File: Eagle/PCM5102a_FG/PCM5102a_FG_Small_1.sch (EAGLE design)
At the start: 28 parts, among them IC1 PSOC_5LP_PROTOTIYPING_KIT, IC2 PCM5102A, IC3 TA48M033F, Q1 20MHz

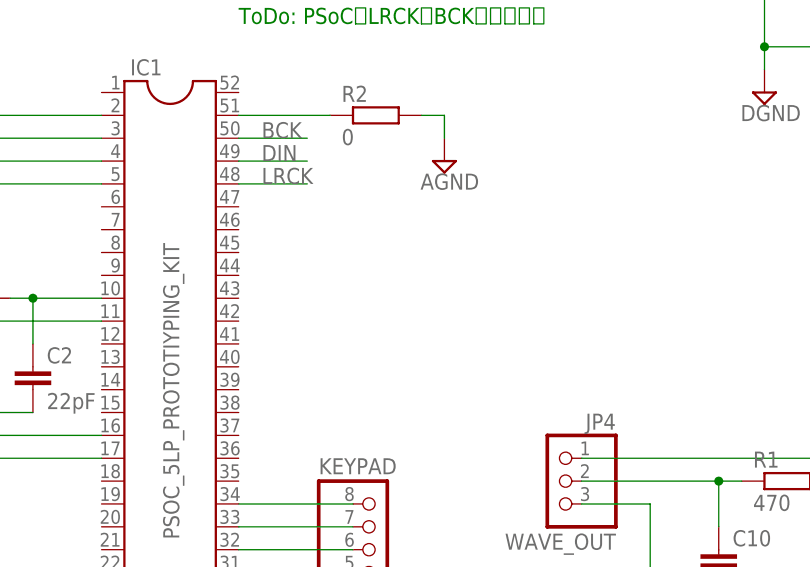
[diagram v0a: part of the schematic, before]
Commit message: 電源電圧測定
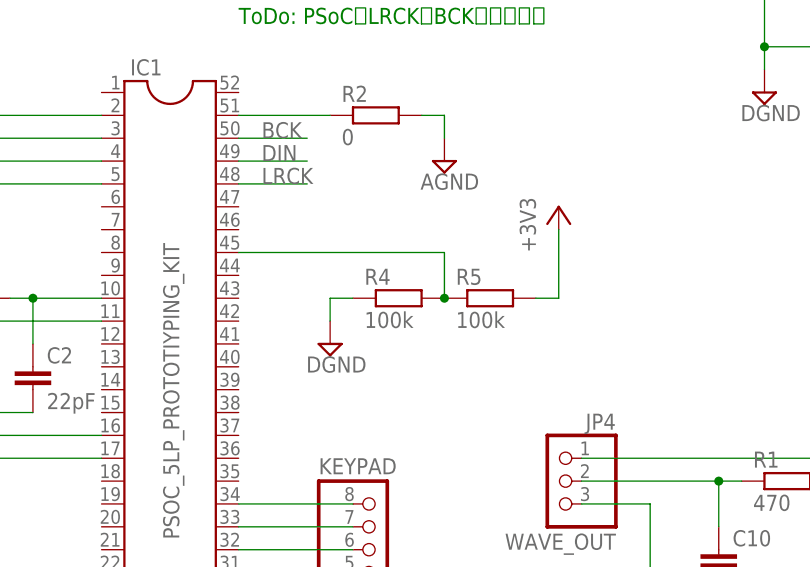
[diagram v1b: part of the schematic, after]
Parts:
- added R4, R5: 100k, resistor:R-EU_0207/7
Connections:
- new net N$19: IC1.45, R4.2, R5.1
- net +3V3: now also R5.2
- net DGND: now also R4.1
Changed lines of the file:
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@@
 <setting verticaltext="up"/>
 </settings>
-<grid distance="0.1" unitdist="inch" unit="inch" style="lines" multiple="1" display="no" altdistance="0.01" altunitdist="inch" altunit="inch"/>
+<grid distance="0.1" unitdist="inch" unit="inch" style="lines" multiple="1" display="yes" altdistance="0.01" altunitdist="inch" altunit="inch"/>
 <layers>
 <layer number="1" name="Top" color="4" fill="1" visible="no" active="no"/>
@@
 <part name="FRAME1" library="frames" deviceset="A4L-LOC" device="" value="PCM5102A_FG"/>
 <part name="C16" library="rcl" deviceset="CPOL-EU" device="E2.5-5" value="10uF"/>
+<part name="R4" library="resistor" deviceset="R-EU_" device="0207/7" value="100k"/>
+<part name="R5" library="resistor" deviceset="R-EU_" device="0207/7" value="100k"/>
+<part name="SUPPLY2" library="supply2" deviceset="DGND" device=""/>
+<part name="+3V5" library="supply1" deviceset="+3V3" device=""/>
 </parts>
 <sheets>
@@
 <instance part="FRAME1" gate="G$1" x="0" y="0"/>
 <instance part="C16" gate="G$1" x="167.64" y="96.52" rot="MR90"/>
+<instance part="R4" gate="G$1" x="104.14" y="91.44"/>
+<instance part="R5" gate="G$1" x="114.3" y="91.44"/>
+<instance part="SUPPLY2" gate="G$1" x="96.52" y="86.36"/>
+<instance part="+3V5" gate="G$1" x="121.92" y="101.6"/>
 </instances>
 <busses>
@@
 <junction x="154.94" y="119.38"/>
 </segment>
+<segment>
+<wire x1="96.52" y1="88.9" x2="96.52" y2="91.44" width="0.1524" layer="91"/>
+<pinref part="R4" gate="G$1" pin="1"/>
+<wire x1="96.52" y1="91.44" x2="99.06" y2="91.44" width="0.1524" layer="91"/>
+<pinref part="SUPPLY2" gate="G$1" pin="DGND"/>
+</segment>
 </net>
 <net name="N$1" class="0">
@@
 <wire x1="208.28" y1="149.86" x2="208.28" y2="139.7" width="0.1524" layer="91"/>
 <junction x="208.28" y="139.7"/>
+</segment>
+<segment>
+<pinref part="R5" gate="G$1" pin="2"/>
+<wire x1="119.38" y1="91.44" x2="121.92" y2="91.44" width="0.1524" layer="91"/>
+<pinref part="+3V5" gate="G$1" pin="+3V3"/>
+<wire x1="121.92" y1="91.44" x2="121.92" y2="99.06" width="0.1524" layer="91"/>
 </segment>
 </net>
@@
 </segment>
 </net>
+<net name="N$19" class="0">
+<segment>
+<pinref part="R4" gate="G$1" pin="2"/>
+<pinref part="R5" gate="G$1" pin="1"/>
+<pinref part="IC1" gate="G$1" pin="45"/>
+<wire x1="86.36" y1="96.52" x2="109.22" y2="96.52" width="0.1524" layer="91"/>
+<wire x1="109.22" y1="96.52" x2="109.22" y2="91.44" width="0.1524" layer="91"/>
+<junction x="109.22" y="91.44"/>
+</segment>
+</net>

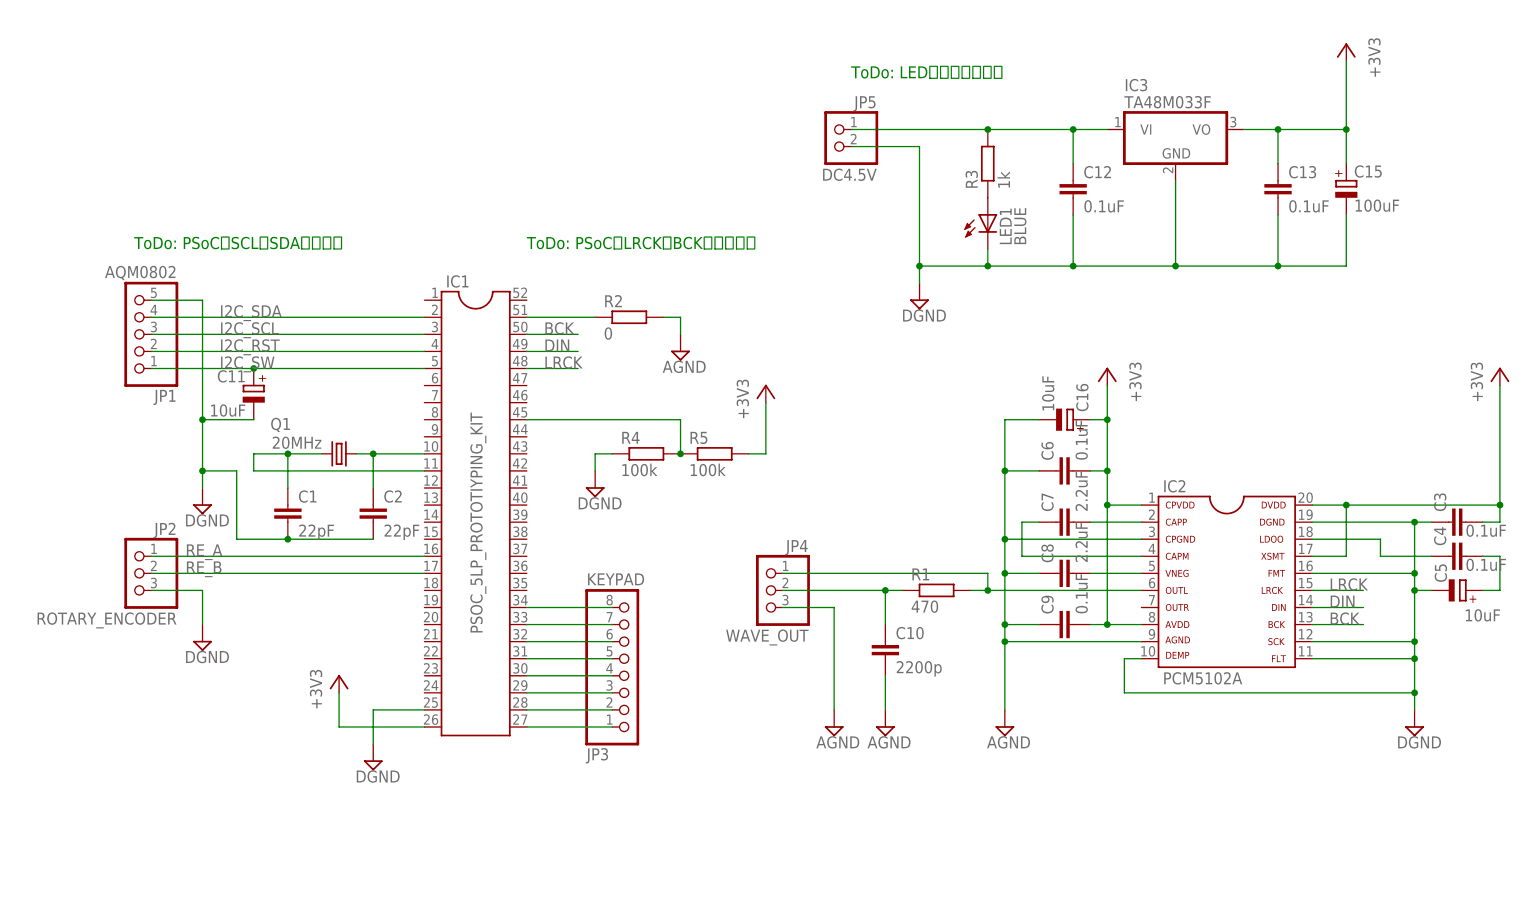
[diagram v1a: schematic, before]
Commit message: LCDのコントラスト調整
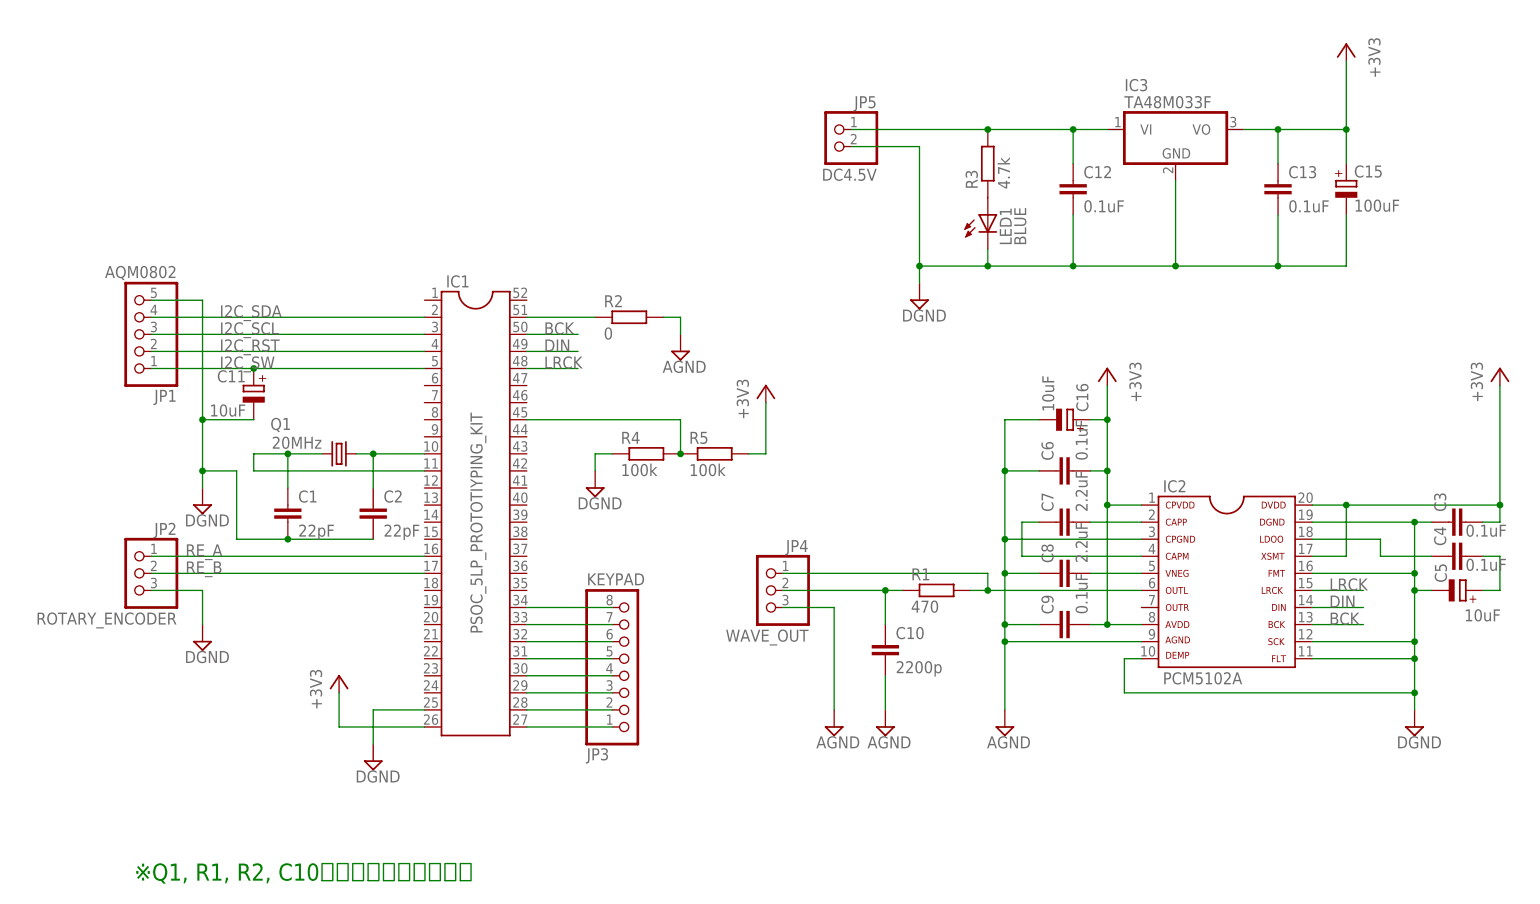
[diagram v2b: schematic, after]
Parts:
- R3: value 1k -> 4.7k
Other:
- note added: "※Q1, R1, R2, C10はピンソケットで実装"
- note removed: "ToDo: LEDの明るさの確認"
- note removed: "ToDo: PSoCでLRCKとBCKを入れ替え"
- note removed: "ToDo: PSoCでSCLとSDA入れ替え"
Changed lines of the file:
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@@
 <setting verticaltext="up"/>
 </settings>
-<grid distance="0.1" unitdist="inch" unit="inch" style="lines" multiple="1" display="yes" altdistance="0.01" altunitdist="inch" altunit="inch"/>
+<grid distance="0.1" unitdist="inch" unit="inch" style="lines" multiple="1" display="no" altdistance="0.01" altunitdist="inch" altunit="inch"/>
 <layers>
 <layer number="1" name="Top" color="4" fill="1" visible="no" active="no"/>
@@
 <part name="+3V2" library="supply1" deviceset="+3V3" device=""/>
 <part name="LED1" library="led" deviceset="LED" device="3MM" value="BLUE"/>
-<part name="R3" library="resistor" deviceset="R-EU_" device="0207/7" value="1k"/>
+<part name="R3" library="resistor" deviceset="R-EU_" device="0207/7" value="4.7k"/>
 <part name="FRAME1" library="frames" deviceset="A4L-LOC" device="" value="PCM5102A_FG"/>
 <part name="C16" library="rcl" deviceset="CPOL-EU" device="E2.5-5" value="10uF"/>
@@
 <sheet>
 <plain>
-<text x="27.94" y="121.92" size="1.778" layer="91">ToDo: PSoCでSCLとSDA入れ替え</text>
-<text x="134.62" y="147.32" size="1.778" layer="91">ToDo: LEDの明るさの確認</text>
-<text x="86.36" y="121.92" size="1.778" layer="91">ToDo: PSoCでLRCKとBCKを入れ替え</text>
+<text x="27.94" y="27.94" size="2.54" layer="91">※Q1, R1, R2, C10はピンソケットで実装</text>
 </plain>
 <instances>

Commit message: 基板図修正: PCM5102a_FG_Small_1.sch/brd
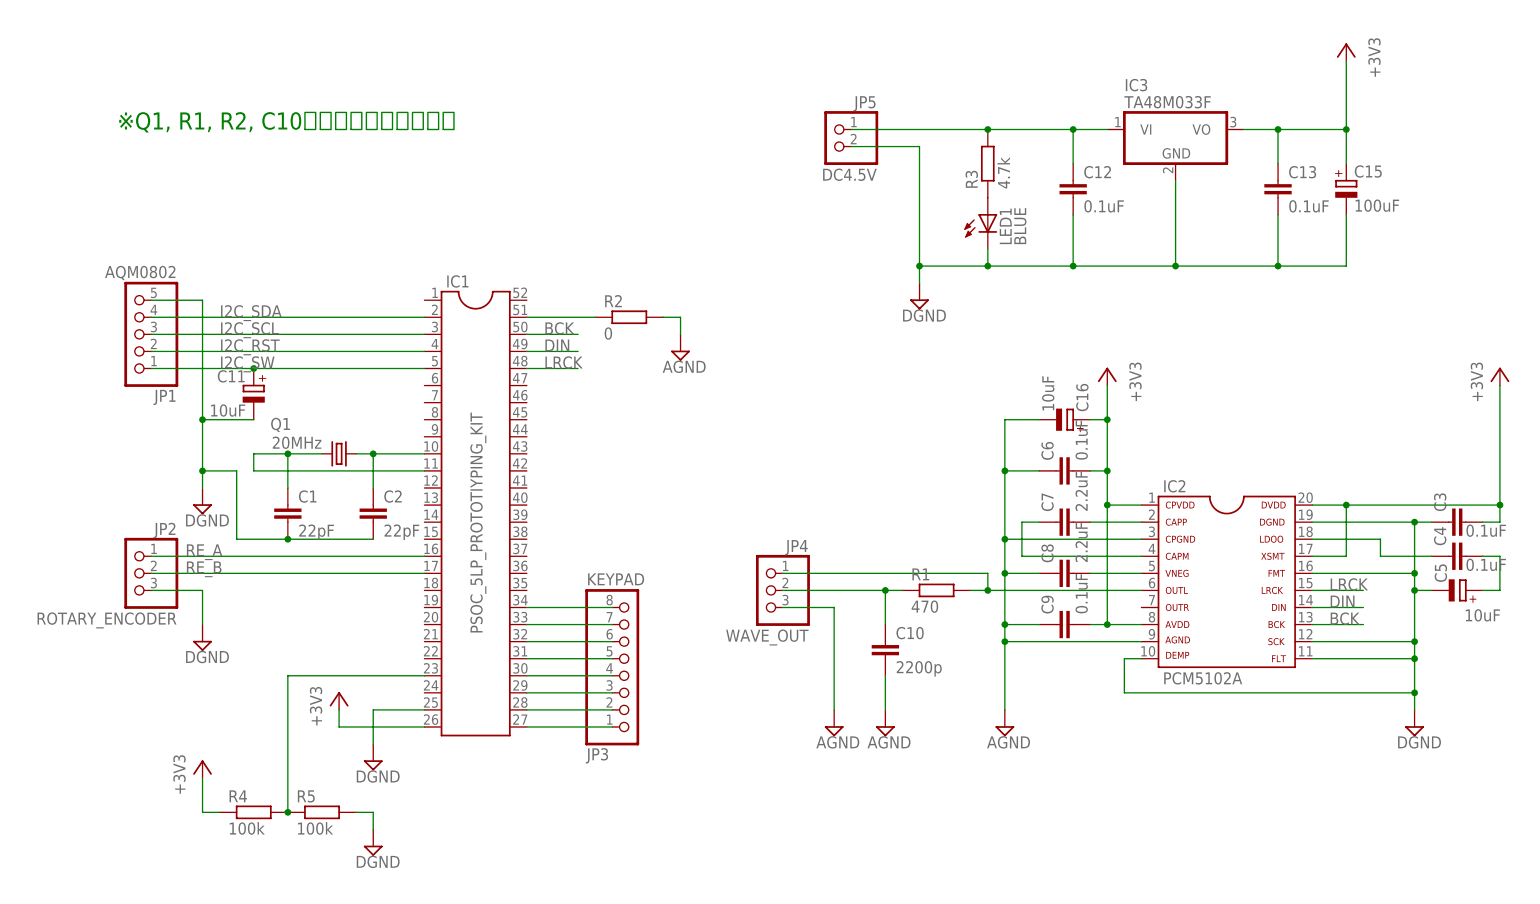
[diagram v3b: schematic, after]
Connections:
- net +3V3: now also R4.1; no longer R5.2
- net DGND: now also R5.2; no longer R4.1
- net N$19: now also IC1.23; no longer IC1.45
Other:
- moved on the sheet: R4, R5
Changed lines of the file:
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@@
 <setting verticaltext="up"/>
 </settings>
-<grid distance="0.1" unitdist="inch" unit="inch" style="lines" multiple="1" display="no" altdistance="0.01" altunitdist="inch" altunit="inch"/>
+<grid distance="0.1" unitdist="inch" unit="inch" style="lines" multiple="1" display="yes" altdistance="0.01" altunitdist="inch" altunit="inch"/>
 <layers>
 <layer number="1" name="Top" color="4" fill="1" visible="no" active="no"/>
@@
 <sheet>
 <plain>
-<text x="27.94" y="27.94" size="2.54" layer="91">※Q1, R1, R2, C10はピンソケットで実装</text>
+<text x="25.4" y="139.7" size="2.54" layer="91">※Q1, R1, R2, C10はピンソケットで実装</text>
 </plain>
 <instances>
@@
 <attribute name="VALUE" x="79.756" y="64.643" size="1.778" layer="96" rot="R90"/>
 </instance>
-<instance part="+3V1" gate="G$1" x="58.42" y="58.42"/>
+<instance part="+3V1" gate="G$1" x="58.42" y="55.88"/>
 <instance part="SUPPLY1" gate="G$1" x="63.5" y="45.72"/>
 <instance part="JP1" gate="A" x="27.94" y="109.22" rot="R180"/>
@@
 <instance part="FRAME1" gate="G$1" x="0" y="0"/>
 <instance part="C16" gate="G$1" x="167.64" y="96.52" rot="MR90"/>
-<instance part="R4" gate="G$1" x="104.14" y="91.44"/>
-<instance part="R5" gate="G$1" x="114.3" y="91.44"/>
-<instance part="SUPPLY2" gate="G$1" x="96.52" y="86.36"/>
-<instance part="+3V5" gate="G$1" x="121.92" y="101.6"/>
+<instance part="R4" gate="G$1" x="45.72" y="38.1"/>
+<instance part="R5" gate="G$1" x="55.88" y="38.1"/>
+<instance part="SUPPLY2" gate="G$1" x="63.5" y="33.02"/>
+<instance part="+3V5" gate="G$1" x="38.1" y="45.72"/>
 </instances>
 <busses>
@@
 </segment>
 <segment>
-<wire x1="96.52" y1="88.9" x2="96.52" y2="91.44" width="0.1524" layer="91"/>
-<pinref part="R4" gate="G$1" pin="1"/>
-<wire x1="96.52" y1="91.44" x2="99.06" y2="91.44" width="0.1524" layer="91"/>
+<pinref part="R5" gate="G$1" pin="2"/>
 <pinref part="SUPPLY2" gate="G$1" pin="DGND"/>
+<wire x1="60.96" y1="38.1" x2="63.5" y2="38.1" width="0.1524" layer="91"/>
+<wire x1="63.5" y1="38.1" x2="63.5" y2="35.56" width="0.1524" layer="91"/>
 </segment>
 </net>
@@
 <wire x1="71.12" y1="50.8" x2="58.42" y2="50.8" width="0.1524" layer="91"/>
 <pinref part="+3V1" gate="G$1" pin="+3V3"/>
-<wire x1="58.42" y1="50.8" x2="58.42" y2="55.88" width="0.1524" layer="91"/>
+<wire x1="58.42" y1="50.8" x2="58.42" y2="53.34" width="0.1524" layer="91"/>
 </segment>
 <segment>
@@
 </segment>
 <segment>
-<pinref part="R5" gate="G$1" pin="2"/>
-<wire x1="119.38" y1="91.44" x2="121.92" y2="91.44" width="0.1524" layer="91"/>
+<pinref part="R4" gate="G$1" pin="1"/>
+<wire x1="40.64" y1="38.1" x2="38.1" y2="38.1" width="0.1524" layer="91"/>
 <pinref part="+3V5" gate="G$1" pin="+3V3"/>
-<wire x1="121.92" y1="91.44" x2="121.92" y2="99.06" width="0.1524" layer="91"/>
+<wire x1="38.1" y1="38.1" x2="38.1" y2="43.18" width="0.1524" layer="91"/>
 </segment>
 </net>
@@
 <pinref part="R4" gate="G$1" pin="2"/>
 <pinref part="R5" gate="G$1" pin="1"/>
-<pinref part="IC1" gate="G$1" pin="45"/>
-<wire x1="86.36" y1="96.52" x2="109.22" y2="96.52" width="0.1524" layer="91"/>
-<wire x1="109.22" y1="96.52" x2="109.22" y2="91.44" width="0.1524" layer="91"/>
-<junction x="109.22" y="91.44"/>
-</segment>
-</net>
+<pinref part="IC1" gate="G$1" pin="23"/>
+<wire x1="71.12" y1="58.42" x2="50.8" y2="58.42" width="0.1524" layer="91"/>
+<wire x1="50.8" y1="58.42" x2="50.8" y2="38.1" width="0.1524" layer="91"/>
+<junction x="50.8" y="38.1"/>
+</segment>
+</net>

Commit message: PCM5102a_FG_Small_1.sch/brd Add: SBD
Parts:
- added D1: 1S4, diode:SCHOTTKY-DIODEDO35-7
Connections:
- net +3V3: now also D1.A
- net DC4.5V: now also D1.C
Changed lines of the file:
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@@
 <setting verticaltext="up"/>
 </settings>
-<grid distance="0.1" unitdist="inch" unit="inch" style="lines" multiple="1" display="yes" altdistance="0.01" altunitdist="inch" altunit="inch"/>
+<grid distance="0.1" unitdist="inch" unit="inch" style="lines" multiple="1" display="no" altdistance="0.01" altunitdist="inch" altunit="inch"/>
 <layers>
 <layer number="1" name="Top" color="4" fill="1" visible="no" active="no"/>
@@
 <part name="SUPPLY2" library="supply2" deviceset="DGND" device=""/>
 <part name="+3V5" library="supply1" deviceset="+3V3" device=""/>
+<part name="D1" library="diode" deviceset="SCHOTTKY-DIODE" device="DO35-7" value="1S4"/>
 </parts>
 <sheets>
@@
 <instance part="SUPPLY2" gate="G$1" x="63.5" y="33.02"/>
 <instance part="+3V5" gate="G$1" x="38.1" y="45.72"/>
+<instance part="D1" gate="G$1" x="182.88" y="152.4" rot="MR0"/>
 </instances>
 <busses>
@@
 <wire x1="208.28" y1="149.86" x2="208.28" y2="139.7" width="0.1524" layer="91"/>
 <junction x="208.28" y="139.7"/>
+<pinref part="D1" gate="G$1" pin="A"/>
+<wire x1="185.42" y1="152.4" x2="198.12" y2="152.4" width="0.1524" layer="91"/>
+<wire x1="198.12" y1="152.4" x2="198.12" y2="139.7" width="0.1524" layer="91"/>
 </segment>
 <segment>
@@
 <wire x1="154.94" y1="139.7" x2="167.64" y2="139.7" width="0.1524" layer="91"/>
 <junction x="154.94" y="139.7"/>
-</segment>
-</net>
+<wire x1="167.64" y1="139.7" x2="167.64" y2="152.4" width="0.1524" layer="91"/>
+<pinref part="D1" gate="G$1" pin="C"/>
+<wire x1="167.64" y1="152.4" x2="180.34" y2="152.4" width="0.1524" layer="91"/>
+</segment>
+</net>
